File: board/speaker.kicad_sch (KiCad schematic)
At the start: 5 parts, among them J1601 SPK_R

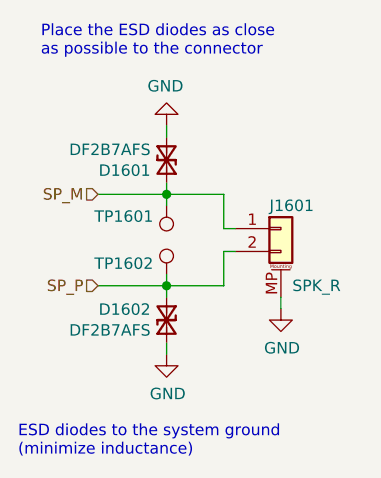
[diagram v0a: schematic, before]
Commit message: Added testpoints and other fixes
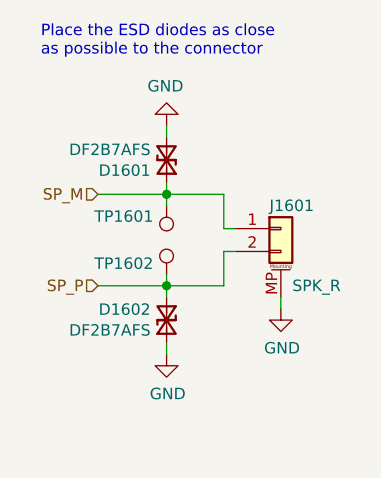
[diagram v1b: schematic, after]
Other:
- note removed: "ESD diodes to the system ground (minimize inductance)"
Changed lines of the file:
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@@
     (stroke (width 0) (type solid) (color 0 0 0 0))
-  )
-  (text "ESD diodes to the system ground\n(minimize inductance)"
-    (at 133.35 124.46 0)
-    (effects (font (size 1.27 1.27)) (justify left bottom))
   )
   (text "Place the ESD diodes as close \nas possible to the connector"
@@
       (effects (font (size 1.27 1.27)) hide)
     )
-    (property "Datasheet" "https://eu.mouser.com/datasheet/2/408/DF2B7AFS_datasheet_en_20180110-1128342.pdf" (id 3) (at 149.86 92.202 90)
+    (property "Datasheet" "~" (id 3) (at 149.86 92.202 90)
       (effects (font (size 1.27 1.27)) hide)
     )
@@
       (effects (font (size 1.27 1.27)) hide)
     )
-    (property "Datasheet" "https://eu.mouser.com/datasheet/2/408/DF2B7AFS_datasheet_en_20180110-1128342.pdf" (id 3) (at 149.86 108.458 90)
+    (property "Datasheet" "~" (id 3) (at 149.86 108.458 90)
       (effects (font (size 1.27 1.27)) hide)
     )
@@
       (effects (font (size 1.27 1.27)) hide)
     )
-    (property "Datasheet" "https://www.molex.com/pdm_docs/sd/533980267_sd.pdf" (id 3) (at 162.56 99.06 0)
-      (effects (font (size 1.27 1.27)) hide)
-    )
+    (property "Datasheet" "~" (id 3) (at 162.56 99.06 0)
+      (effects (font (size 1.27 1.27)) hide)
+    )
